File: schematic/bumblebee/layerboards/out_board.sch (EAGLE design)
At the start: 10 parts, among them IC1 REG1117, P3 B7B-EH-A, P5 B3B-EH-A

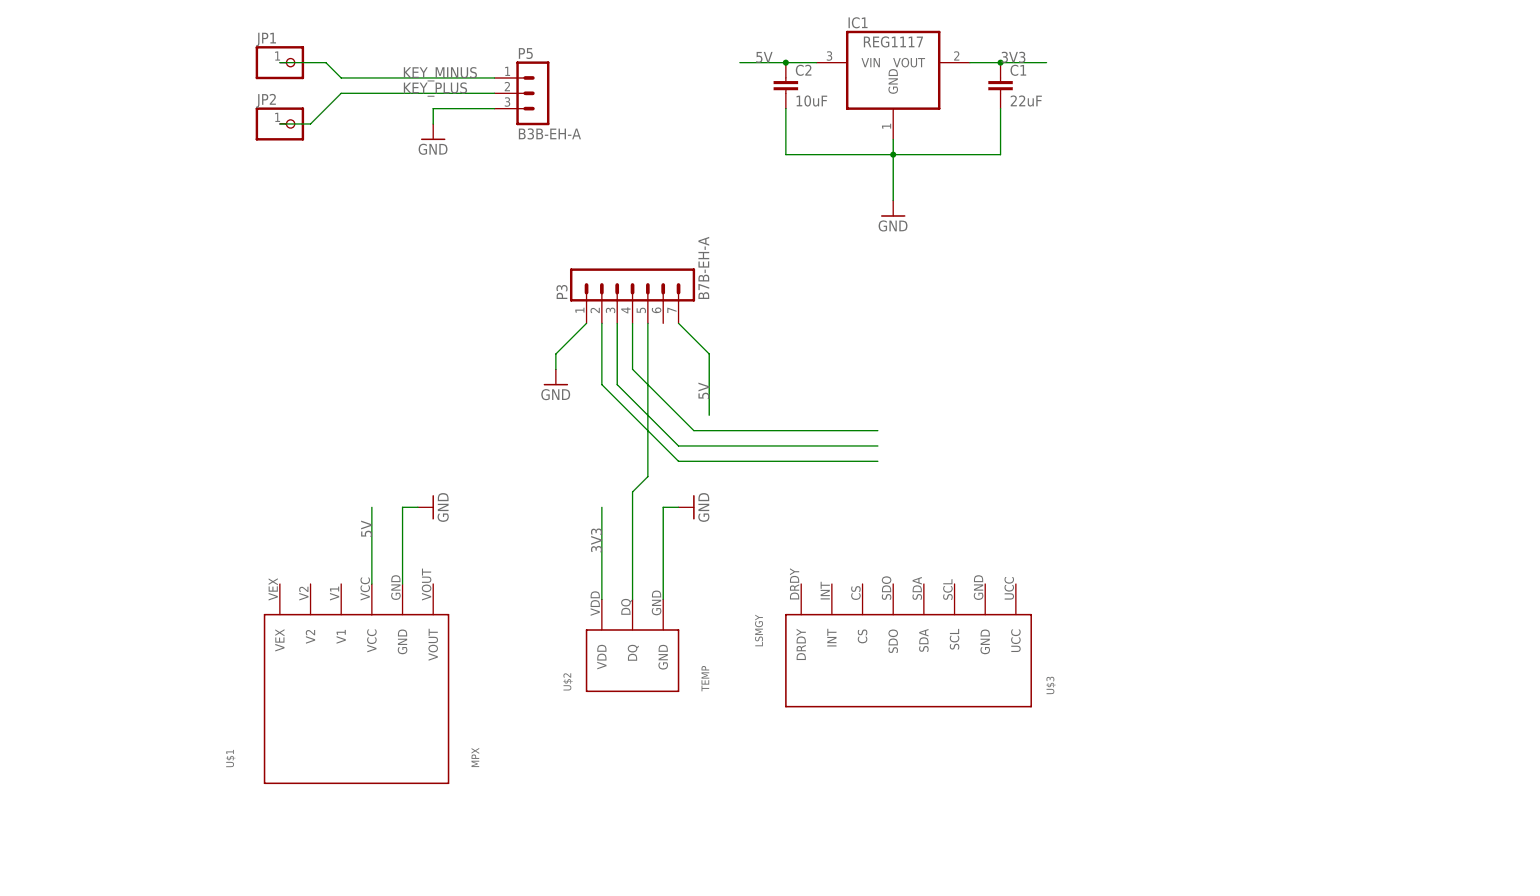
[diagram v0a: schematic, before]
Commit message: Добавлена плата АЦП на CCU Сделана и разведена внешняя плата Кое-что сделал в либе
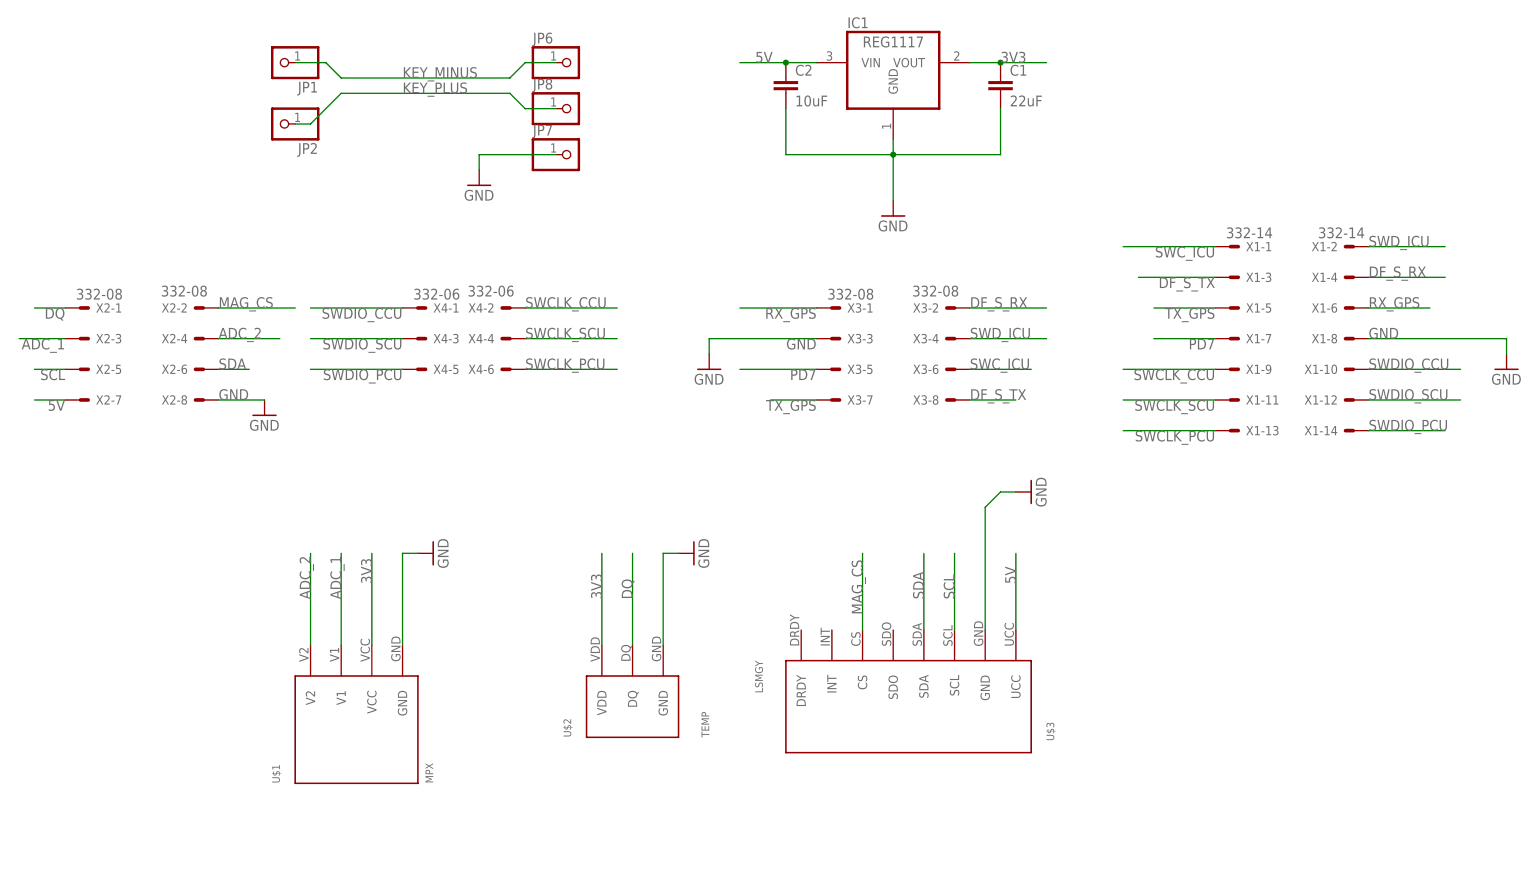
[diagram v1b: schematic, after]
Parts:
- removed P3: B7B-EH-A, con-jst-eh:B7B-EH-A
- removed P5: B3B-EH-A, con-jst-eh:B3B-EH-A
- added JP6, JP7, JP8: (no value), pinhead:PINHD-1X1
- added X1: 332-14, con-garry:332-14
- added X2, X3: 332-08, con-garry:332-08
- added X4: 332-06, con-garry:332-06
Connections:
- removed net MAG_CLOCK: P3.3
- removed net MAG_DATA: P3.4
- removed net N$1: P3.2
- removed net N$2: P3.5, U$2.DQ
- new net ADC_1: U$1.V1, X2-3.S
- new net ADC_2: U$1.V2, X2-4.S
- new net DF_S_RX: X1-4.S, X3-2.S
- new net DF_S_TX: X1-3.S, X3-8.S
- new net DQ: U$2.DQ, X2-1.S
- new net MAG_CS: U$3.CS, X2-2.S
- new net PD7: X1-7.S, X3-5.S
- new net RX_GPS: X1-6.S, X3-1.S
- new net SCL: U$3.SCL, X2-5.S
- new net SDA: U$3.SDA, X2-6.S
- new net SWCLK_CCU: X1-9.S, X4-2.S
- new net SWCLK_PCU: X1-13.S, X4-6.S
- new net SWCLK_SCU: X1-11.S, X4-4.S
- new net SWC_ICU: X1-1.S, X3-6.S
- new net SWDIO_CCU: X1-10.S, X4-1.S
- new net SWDIO_PCU: X1-14.S, X4-5.S
- new net SWDIO_SCU: X1-12.S, X4-3.S
- new net SWD_ICU: X1-2.S, X3-4.S
- new net TX_GPS: X1-5.S, X3-7.S
- net 3V3: now also U$1.VCC
- net 5V: now also U$3.UCC, X2-7.S; no longer P3.7, U$1.VCC
- net GND: now also JP7.1, U$3.GND, X1-8.S, X2-8.S, X3-3.S; no longer P3.1, P5.3
- net KEY_MINUS: now also JP6.1; no longer P5.1
- net KEY_PLUS: now also JP8.1; no longer P5.2
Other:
- moved on the sheet: JP1, JP2, U$2, U$3

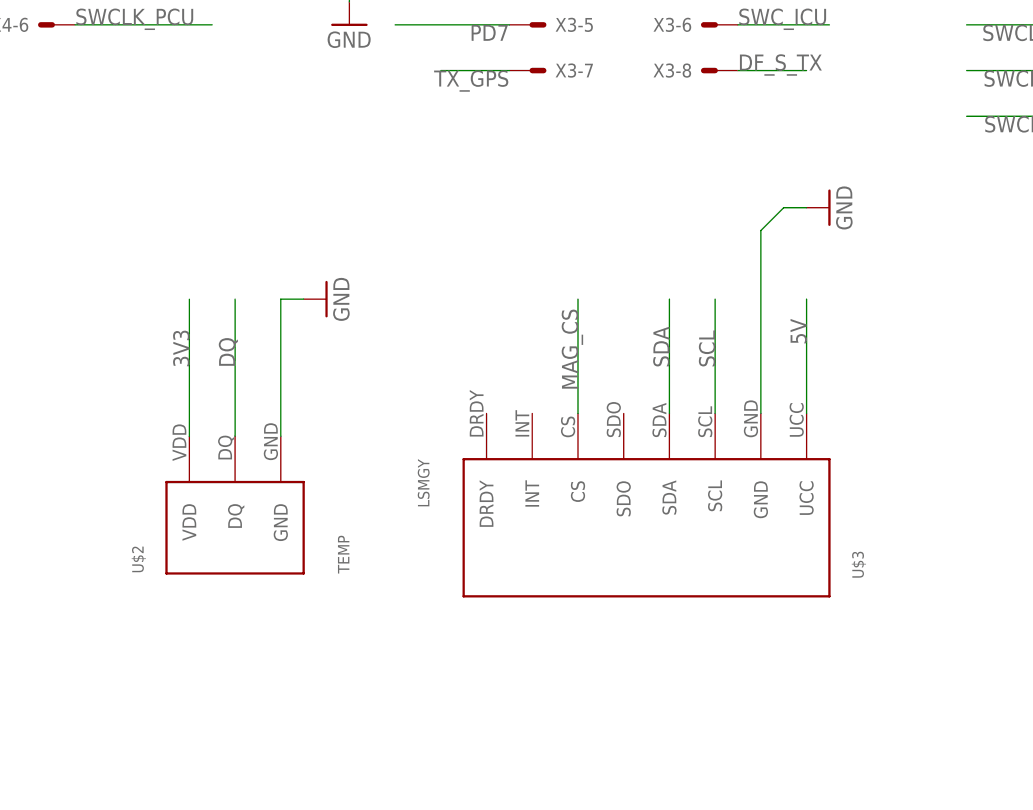
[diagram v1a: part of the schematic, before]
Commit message: Все платы готовы и отправлены в резонит
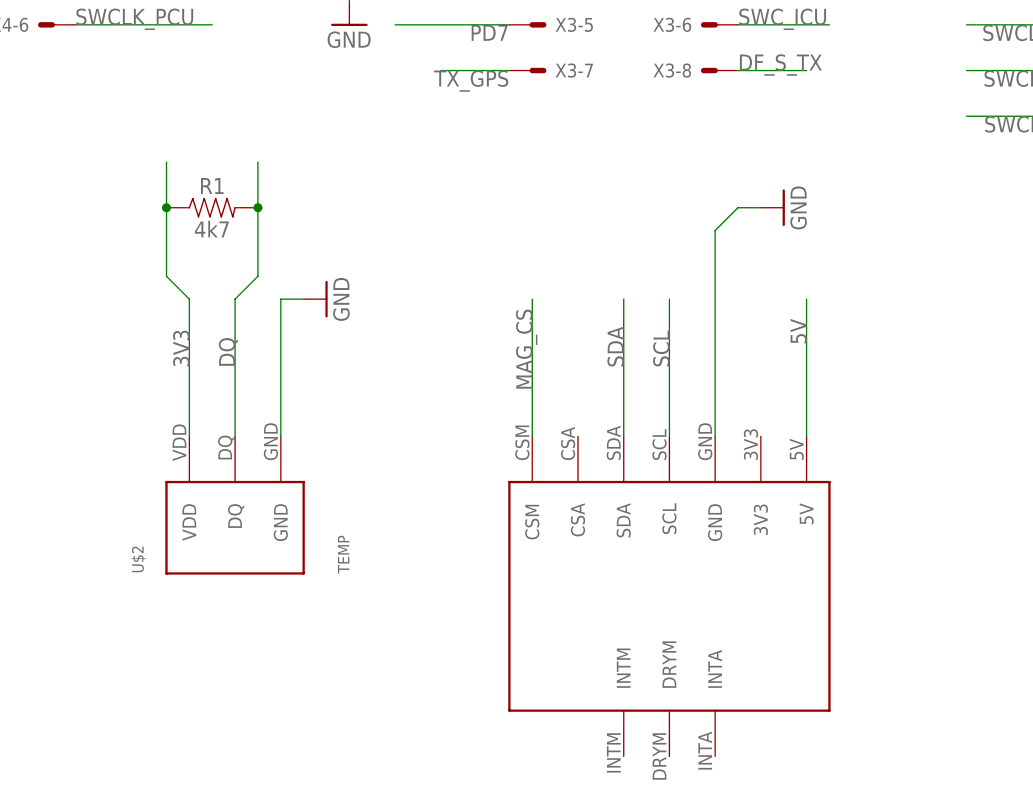
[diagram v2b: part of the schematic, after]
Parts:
- added R1: 4k7, SparkFun-Resistors:RESISTORAXIAL-0.3
- U$3: value LSMGY -> LSM303C; device bluepill:LSMGY -> bluepill:LSM303C
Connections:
- net 3V3: now also R1.1
- net 5V: now also U$3.5V; no longer U$3.UCC
- net DQ: now also R1.2
- net MAG_CS: now also U$3.CSM; no longer U$3.CS
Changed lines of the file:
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@@
 <parts>
 <part name="U$2" library="bluepill" deviceset="TEMP" device=""/>
-<part name="U$3" library="bluepill" deviceset="LSMGY" device=""/>
 <part name="JP1" library="pinhead" library_urn="urn:adsk.eagle:library:325" deviceset="PINHD-1X1" device="" package3d_urn="urn:adsk.eagle:package:22485/2"/>
 <part name="JP2" library="pinhead" library_urn="urn:adsk.eagle:library:325" deviceset="PINHD-1X1" device="" package3d_urn="urn:adsk.eagle:package:22485/2"/>
@@
 <part name="GND6" library="supply1" library_urn="urn:adsk.eagle:library:371" deviceset="GND" device=""/>
 <part name="GND8" library="supply1" library_urn="urn:adsk.eagle:library:371" deviceset="GND" device=""/>
+<part name="U$3" library="bluepill" deviceset="LSM303C" device=""/>
+<part name="R1" library="SparkFun-Resistors" deviceset="RESISTOR" device="AXIAL-0.3" value="4k7"/>
 </parts>
 <sheets>
@@
 <attribute name="VALUE" x="20.32" y="-66.04" size="1.27" layer="96" rot="R90"/>
 </instance>
-<instance part="U$3" gate="G$1" x="55.88" y="-63.5" smashed="yes" rot="R270">
-<attribute name="NAME" x="76.2" y="-63.5" size="1.27" layer="95" rot="R270"/>
-<attribute name="VALUE" x="27.94" y="-53.34" size="1.27" layer="96" rot="R270"/>
-</instance>
 <instance part="JP1" gate="G$1" x="-50.8" y="45.72" smashed="yes" rot="R180">
 <attribute name="NAME" x="-44.45" y="42.545" size="1.778" layer="95" rot="R180"/>
@@
 <attribute name="VALUE" x="-8.89" y="33.02" size="1.778" layer="96"/>
 </instance>
-<instance part="GND4" gate="1" x="73.66" y="-25.4" smashed="yes" rot="R90">
-<attribute name="VALUE" x="76.2" y="-27.94" size="1.778" layer="96" rot="R90"/>
+<instance part="GND4" gate="1" x="68.58" y="-25.4" smashed="yes" rot="R90">
+<attribute name="VALUE" x="71.12" y="-27.94" size="1.778" layer="96" rot="R90"/>
 </instance>
 <instance part="U$1" gate="G$1" x="-38.1" y="-63.5" smashed="yes" rot="R90">
@@
 <instance part="GND8" gate="1" x="20.32" y="-5.08" smashed="yes">
 <attribute name="VALUE" x="17.78" y="-7.62" size="1.778" layer="96"/>
+</instance>
+<instance part="U$3" gate="G$1" x="55.88" y="-68.58" smashed="yes" rot="R270"/>
+<instance part="R1" gate="G$1" x="5.08" y="-25.4" smashed="yes">
+<attribute name="NAME" x="5.08" y="-23.876" size="1.778" layer="95" font="vector" align="bottom-center"/>
+<attribute name="VALUE" x="5.08" y="-26.924" size="1.778" layer="96" font="vector" align="top-center"/>
 </instance>
 </instances>
@@
 </segment>
 <segment>
+<wire x1="60.96" y1="-50.8" x2="60.96" y2="-27.94" width="0.1524" layer="91"/>
+<wire x1="60.96" y1="-27.94" x2="63.5" y2="-25.4" width="0.1524" layer="91"/>
+<wire x1="63.5" y1="-25.4" x2="66.04" y2="-25.4" width="0.1524" layer="91"/>
+<pinref part="GND4" gate="1" pin="GND"/>
 <pinref part="U$3" gate="G$1" pin="GND"/>
-<wire x1="66.04" y1="-48.26" x2="66.04" y2="-27.94" width="0.1524" layer="91"/>
-<wire x1="66.04" y1="-27.94" x2="68.58" y2="-25.4" width="0.1524" layer="91"/>
-<wire x1="68.58" y1="-25.4" x2="71.12" y2="-25.4" width="0.1524" layer="91"/>
-<pinref part="GND4" gate="1" pin="GND"/>
 </segment>
 <segment>
@@
 <wire x1="2.54" y1="-50.8" x2="2.54" y2="-35.56" width="0.1524" layer="91"/>
 <label x="2.54" y="-43.18" size="1.778" layer="95" rot="R90"/>
+<wire x1="2.54" y1="-35.56" x2="0" y2="-33.02" width="0.1524" layer="91"/>
+<pinref part="R1" gate="G$1" pin="1"/>
+<wire x1="0" y1="-33.02" x2="0" y2="-25.4" width="0.1524" layer="91"/>
+<wire x1="0" y1="-25.4" x2="0" y2="-20.32" width="0.1524" layer="91"/>
+<junction x="0" y="-25.4"/>
 </segment>
 <segment>
@@
 </segment>
 <segment>
-<pinref part="U$3" gate="G$1" pin="UCC"/>
-<wire x1="71.12" y1="-48.26" x2="71.12" y2="-35.56" width="0.1524" layer="91"/>
+<wire x1="71.12" y1="-50.8" x2="71.12" y2="-35.56" width="0.1524" layer="91"/>
 <label x="71.12" y="-40.64" size="1.778" layer="95" rot="R90"/>
+<pinref part="U$3" gate="G$1" pin="5V"/>
 </segment>
 <segment>
@@
 <net name="SDA" class="0">
 <segment>
+<wire x1="50.8" y1="-50.8" x2="50.8" y2="-35.56" width="0.1524" layer="91"/>
+<label x="50.8" y="-43.18" size="1.778" layer="95" rot="R90"/>
 <pinref part="U$3" gate="G$1" pin="SDA"/>
-<wire x1="55.88" y1="-48.26" x2="55.88" y2="-35.56" width="0.1524" layer="91"/>
-<label x="55.88" y="-43.18" size="1.778" layer="95" rot="R90"/>
 </segment>
 <segment>
@@
 <net name="SCL" class="0">
 <segment>
+<wire x1="55.88" y1="-50.8" x2="55.88" y2="-35.56" width="0.1524" layer="91"/>
+<label x="55.88" y="-43.18" size="1.778" layer="95" rot="R90"/>
 <pinref part="U$3" gate="G$1" pin="SCL"/>
-<wire x1="60.96" y1="-48.26" x2="60.96" y2="-35.56" width="0.1524" layer="91"/>
-<label x="60.96" y="-43.18" size="1.778" layer="95" rot="R90"/>
 </segment>
 <segment>
@@
 </segment>
 <segment>
-<pinref part="U$3" gate="G$1" pin="CS"/>
-<wire x1="45.72" y1="-48.26" x2="45.72" y2="-35.56" width="0.1524" layer="91"/>
-<label x="45.72" y="-45.72" size="1.778" layer="95" rot="R90"/>
+<wire x1="40.64" y1="-50.8" x2="40.64" y2="-35.56" width="0.1524" layer="91"/>
+<label x="40.64" y="-45.72" size="1.778" layer="95" rot="R90"/>
+<pinref part="U$3" gate="G$1" pin="CSM"/>
 </segment>
 </net>
@@
 <wire x1="7.62" y1="-50.8" x2="7.62" y2="-35.56" width="0.1524" layer="91"/>
 <label x="7.62" y="-43.18" size="1.778" layer="95" rot="R90"/>
-</segment>
-</net>
+<wire x1="7.62" y1="-35.56" x2="10.16" y2="-33.02" width="0.1524" layer="91"/>
+<pinref part="R1" gate="G$1" pin="2"/>
+<wire x1="10.16" y1="-33.02" x2="10.16" y2="-25.4" width="0.1524" layer="91"/>
+<wire x1="10.16" y1="-25.4" x2="10.16" y2="-20.32" width="0.1524" layer="91"/>
+<junction x="10.16" y="-25.4"/>
+</segment>
+</net>
